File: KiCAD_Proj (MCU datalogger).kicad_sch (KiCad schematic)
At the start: 25 parts, among them U1 24LC1025-I_SM, U2 DS1337S_, U3 24LC1025-I_SM, U4 ATMEGA328P-AU, Y1 32.768 KHz, Y2 16MHz

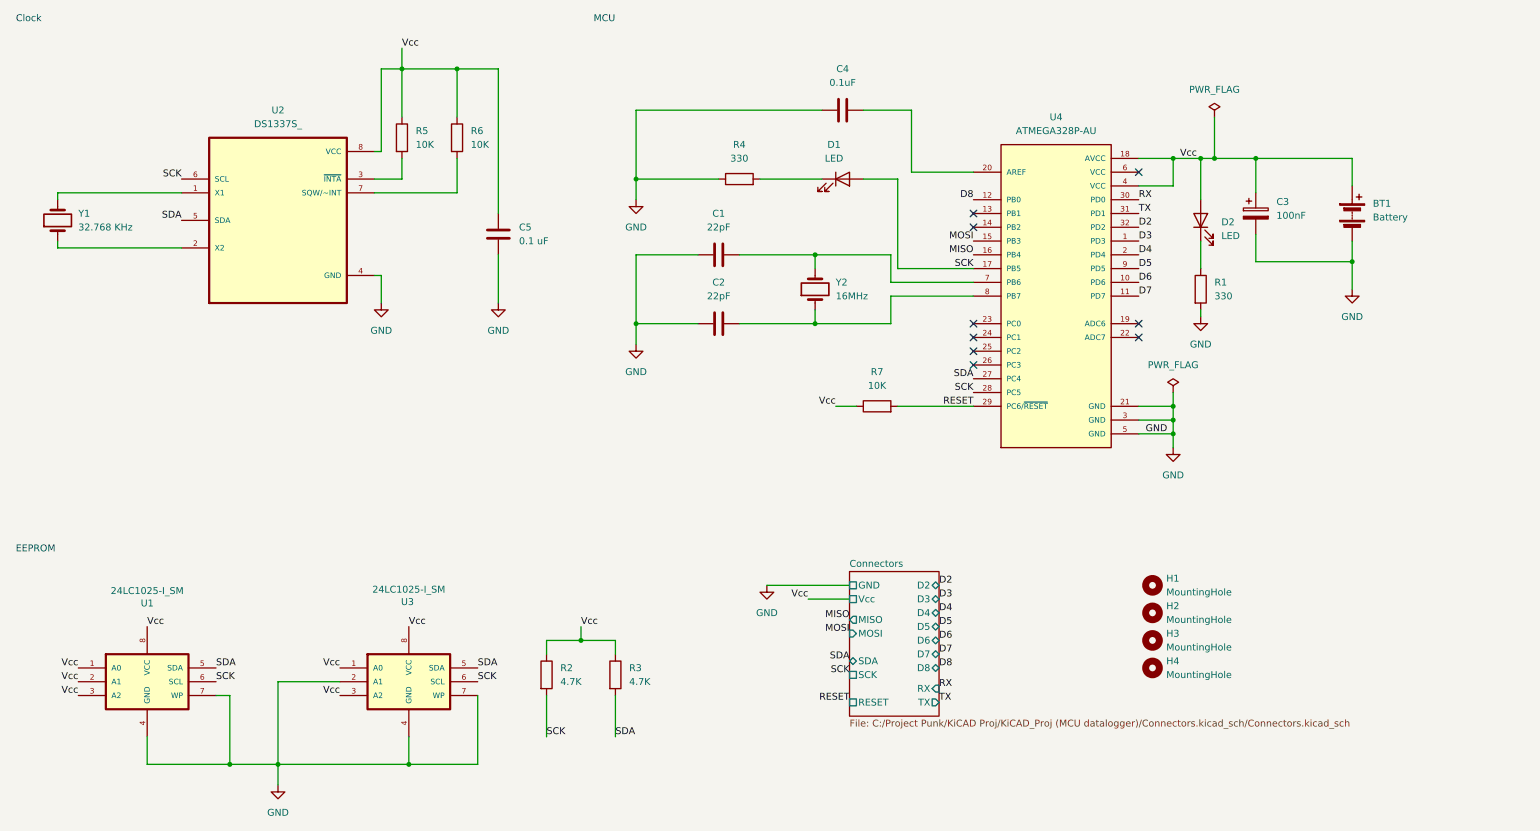
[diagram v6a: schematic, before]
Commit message: Allocated GND and Vcc nets to the Power net class.
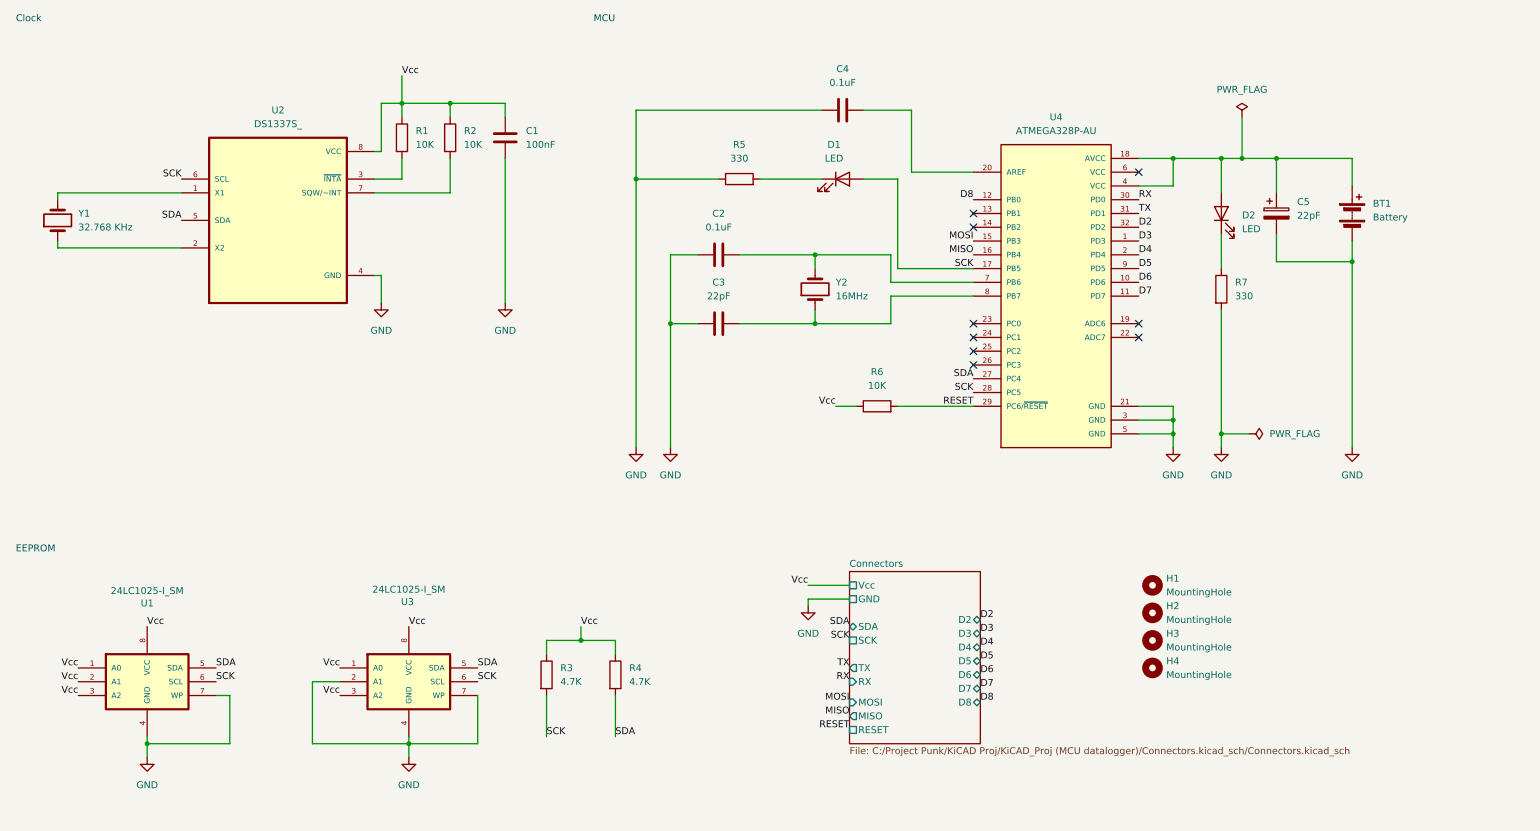
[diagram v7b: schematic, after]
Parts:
- BT1: footprint (none) -> Connector_PinHeader_2.54mm:PinHeader_1x02_P2.54mm_Vertical
- C1: renamed from C5; value 0.1 uF -> 100nF
- C2: renamed from C1; value 22pF -> 0.1uF
- C5: renamed from C3; value 100nF -> 22pF
- renumbered C2 to C3, R5 to R1, R6 to R2, R2 to R3, R3 to R4, R4 to R5, R7 to R6, R1 to R7
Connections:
- net Vcc: no longer BT1.1 (+), C5.1, D2.2 (A), U4.18 (AVCC), U4.4 (VCC)
- new net: BT1.1 (+), C5.1, D2.2 (A), U4.18 (AVCC), U4.4 (VCC)
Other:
- moved on the sheet: C1, C5, D2, R2, R7

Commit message: Allocated GND and Vcc nets to the Power net class.
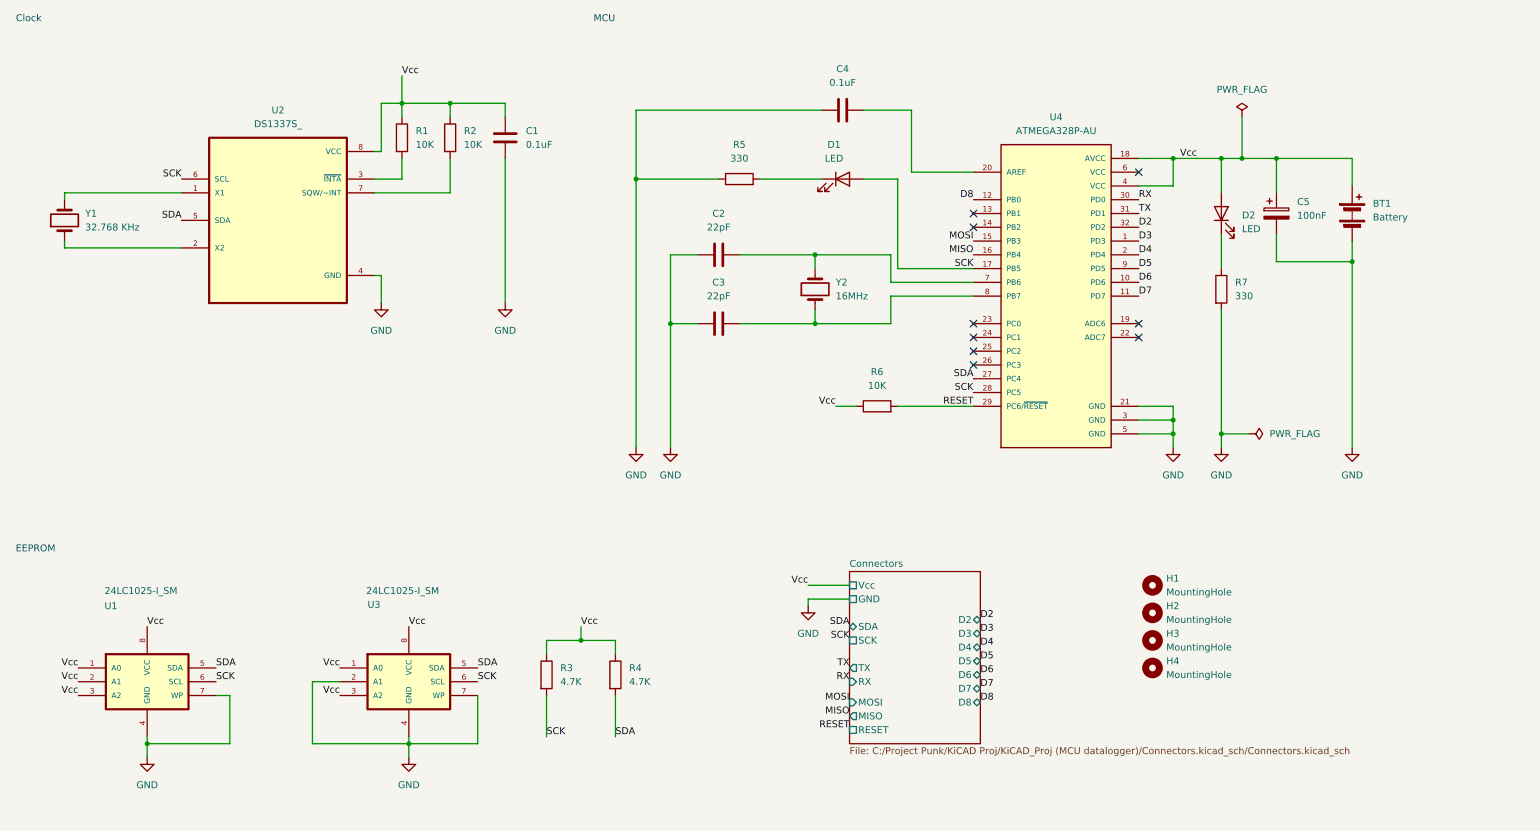
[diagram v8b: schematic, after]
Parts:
- C1: value 100nF -> 0.1uF
- C2: value 0.1uF -> 22pF
- C5: value 22pF -> 100nF
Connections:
- net Vcc: now also BT1.1 (+), C5.1, D2.2 (A), U4.18 (AVCC), U4.4 (VCC)
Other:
- moved on the sheet: Y1
